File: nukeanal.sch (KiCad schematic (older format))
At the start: 84 parts, among them K1 CONN_3, P1 BNC, P4 CONN_2, Q1 VN3205N8-G, Q2 MMBT5089, Q3 LP0701, Q4 MMBT5089, Q5 BSS83, Q6 BSS83, SW1 ONOFF, U1 OPA2365, U10 74HC14, U11 74HC74, U2 LE33CD, U3 MIC5219YM5TR, U4 REF5045, U5 MIC5209-2.5, U6 OPA2365, U7 74HC14, U8 LM311N, U9 AD7983

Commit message: jerry fixed regulator
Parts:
- removed U2: LE33CD, Power_Integrations:SO-8, symbol LE33-SO8
- added P?: CONN_1, symbol CONN_1
- added P?: CONN_6, symbol CONN_6
- added P?: DE-9F, symbol CONN_9
- added U2: MIC5209-3.3, 111kicad-jake:SOT-223-3, symbol 7805
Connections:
- net +5.15V is gone; now on net +5.25V: CU4.1, U4.2 (VIN)
- net +3.3V: now also U2.VO
- net BATT+: now also U2.VI; no longer U3.1 (VIN)
- net GND: now also P?.1, P?.1 (P1), P?.2, P?.2 (P2), P?.3 (P3), P?.4 (P4), P?.5 (P5), U2.GND
- net SCLK: now also P?.4, P?.7 (P7)
- net SDO: now also P?.3, P?.6 (P6)
- net TEST: now also P?.1
- net ~CE: now also P?.5, P?.8 (P8)
- net ~REQ: now also P?.6, P?.9 (P9)
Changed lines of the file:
@@
 TEMP
-$Comp
-L +5.15V #PWR11
-U 1 1 534107A8
-P 4100 1500
-F 0 "#PWR11" H 4100 1460 30  0001 C CNN
-F 1 "+5.15V" H 4100 1610 30  0000 C CNN
-F 2 "" H 4100 1500 60  0001 C CNN
-F 3 "" H 4100 1500 60  0000 C CNN
-	1    4100 1500
-	1    0    0    -1
-$EndComp
 $Comp
 L C C3
@@
 L GND #PWR8
 U 1 1 53410E43
-P 3500 5200
-F 0 "#PWR8" H 3500 5200 30  0001 C CNN
-F 1 "GND" H 3500 5130 30  0001 C CNN
-F 2 "" H 3500 5200 60  0001 C CNN
-F 3 "" H 3500 5200 60  0000 C CNN
-	1    3500 5200
+P 3200 5150
+F 0 "#PWR8" H 3200 5150 30  0001 C CNN
+F 1 "GND" H 3200 5080 30  0001 C CNN
+F 2 "" H 3200 5150 60  0001 C CNN
+F 3 "" H 3200 5150 60  0000 C CNN
+	1    3200 5150
 	1    0    0    -1
 $EndComp
@@
 Text Notes 13750 4650 0    60   ~ 0
 Spare
-$Comp
-L LE33-SO8 U2
-U 1 1 534125E6
-P 3200 4950
-F 0 "U2" H 3200 4650 60  0000 C CNN
-F 1 "LE33CD" H 3200 5150 60  0000 C CNN
-F 2 "Power_Integrations:SO-8" H 3200 4950 60  0001 C CNN
-F 3 "" H 3200 4950 60  0000 C CNN
-	1    3200 4950
-	1    0    0    -1
-$EndComp
-$Comp
-L GND #PWR5
-U 1 1 53412625
-P 2750 5050
-F 0 "#PWR5" H 2750 5050 30  0001 C CNN
-F 1 "GND" H 2750 4980 30  0001 C CNN
-F 2 "" H 2750 5050 60  0001 C CNN
-F 3 "" H 2750 5050 60  0000 C CNN
-	1    2750 5050
-	1    0    0    -1
-$EndComp
 Text Notes 3850 5600 0    60   ~ 0
 change to 5.25v Vdd and -0.25v Vee
@@
 	7350 3750 8300 3750
 Wire Wire Line
-	7350 3350 7100 3350
+	7100 3350 7350 3350
 Wire Wire Line
 	8150 2750 8150 3550
@@
 Wire Wire Line
 	3650 1500 4350 1500
-Connection ~ 2900 5050
-Connection ~ 3500 5050
-Connection ~ 3500 5150
-Wire Wire Line
-	3500 4950 3500 5200
 Wire Wire Line
 	6200 2800 6200 3350
-Wire Wire Line
-	3500 4850 4100 4850
 Wire Wire Line
 	4000 4950 4100 4950
@@
 Wire Wire Line
 	5900 1650 5900 1400
-Wire Wire Line
-	2900 4950 2900 5050
-Wire Wire Line
-	2900 5050 2750 5050
-Wire Wire Line
-	2800 4850 2900 4850
 Wire Wire Line
 	4100 5050 3850 5050
@@
 Wire Wire Line
 	850  3350 1500 3350
+$Comp
+L +5.25V #PWR?
+U 1 1 534622F8
+P 4100 1500
+F 0 "#PWR?" H 4100 1630 20  0001 C CNN
+F 1 "+5.25V" H 4100 1600 30  0000 C CNN
+F 2 "" H 4100 1500 60  0000 C CNN
+F 3 "" H 4100 1500 60  0000 C CNN
+	1    4100 1500
+	1    0    0    -1
+$EndComp
+$Comp
+L 7805 U2
+U 1 1 5346230A
+P 3200 4900
+F 0 "U2" H 3350 4704 60  0000 C CNN
+F 1 "MIC5209-3.3" H 3200 5100 60  0000 C CNN
+F 2 "111kicad-jake:SOT-223-3" H 3200 4550 60  0001 C CNN
+F 3 "" H 3200 4900 60  0000 C CNN
+	1    3200 4900
+	-1   0    0    -1
+$EndComp
+Wire Wire Line
+	3850 4850 3600 4850
+$Comp
+L CONN_1 P?
+U 1 1 53462529
+P 13600 2900
+F 0 "P?" H 13680 2900 40  0000 L CNN
+F 1 "CONN_1" H 13600 2955 30  0001 C CNN
+F 2 "" H 13600 2900 60  0000 C CNN
+F 3 "" H 13600 2900 60  0000 C CNN
+	1    13600 2900
+	0    1    1    0
+$EndComp
+$Comp
+L CONN_6 P?
+U 1 1 534625CF
+P 15700 4900
+F 0 "P?" V 15650 4900 60  0000 C CNN
+F 1 "CONN_6" V 15750 4900 60  0000 C CNN
+F 2 "" H 15700 4900 60  0000 C CNN
+F 3 "" H 15700 4900 60  0000 C CNN
+	1    15700 4900
+	1    0    0    -1
+$EndComp
+$Comp
+L CONN_9 P?
+U 1 1 53462603
+P 15750 3950
+F 0 "P?" V 15700 3950 60  0000 C CNN
+F 1 "DE-9F" V 15800 3950 60  0000 C CNN
+F 2 "" H 15750 3950 60  0000 C CNN
+F 3 "" H 15750 3950 60  0000 C CNN
+	1    15750 3950
+	1    0    0    -1
+$EndComp
+Text Label 14900 5050 2    60   ~ 0
+~CE
+Wire Wire Line
+	14900 5050 15350 5050
+Text Label 15200 4950 2    60   ~ 0
+SCLK
+Wire Wire Line
+	15350 4950 15200 4950
+Text Label 14750 4850 2    60   ~ 0
+SDO
+Wire Wire Line
+	14750 4850 15350 4850
+Text Label 15050 5200 2    60   ~ 0
+~REQ
+Wire Wire Line
+	15050 5200 15350 5200
+Wire Wire Line
+	15350 5200 15350 5150
+$Comp
+L GND #PWR?
+U 1 1 53462BE7
+P 15200 4650
+F 0 "#PWR?" H 15200 4650 30  0001 C CNN
+F 1 "GND" H 15200 4580 30  0001 C CNN
+F 2 "" H 15200 4650 60  0000 C CNN
+F 3 "" H 15200 4650 60  0000 C CNN
+	1    15200 4650
+	1    0    0    -1
+$EndComp
+Wire Wire Line
+	15200 4650 15350 4650
+Wire Wire Line
+	15350 4650 15350 4750
+Connection ~ 15350 4650
+Text Label 15150 4050 2    60   ~ 0
+SDO
+Wire Wire Line
+	15150 4050 15400 4050
+$Comp
+L GND #PWR?
+U 1 1 53462E3D
+P 15250 3600
+F 0 "#PWR?" H 15250 3600 30  0001 C CNN
+F 1 "GND" H 15250 3530 30  0001 C CNN
+F 2 "" H 15250 3600 60  0000 C CNN
+F 3 "" H 15250 3600 60  0000 C CNN
+	1    15250 3600
+	1    0    0    -1
+$EndComp
+Wire Wire Line
+	15250 3600 15400 3600
+Wire Wire Line
+	15400 3550 15400 3950
+Connection ~ 15400 3650
+Connection ~ 15400 3750
+Connection ~ 15400 3850
+Connection ~ 15400 3950
+Connection ~ 15400 3600
+Connection ~ 15400 3550
+Text Label 15100 4150 2    60   ~ 0
+SCLK
+Wire Wire Line
+	15100 4150 15400 4150
+Text Label 15100 4250 2    60   ~ 0
+~CE
+Wire Wire Line
+	15100 4250 15400 4250
+Text Label 15150 4400 2    60   ~ 0
+~REQ
+Wire Wire Line
+	15150 4400 15400 4400
+Wire Wire Line
+	15400 4400 15400 4350
 $EndSCHEMATC

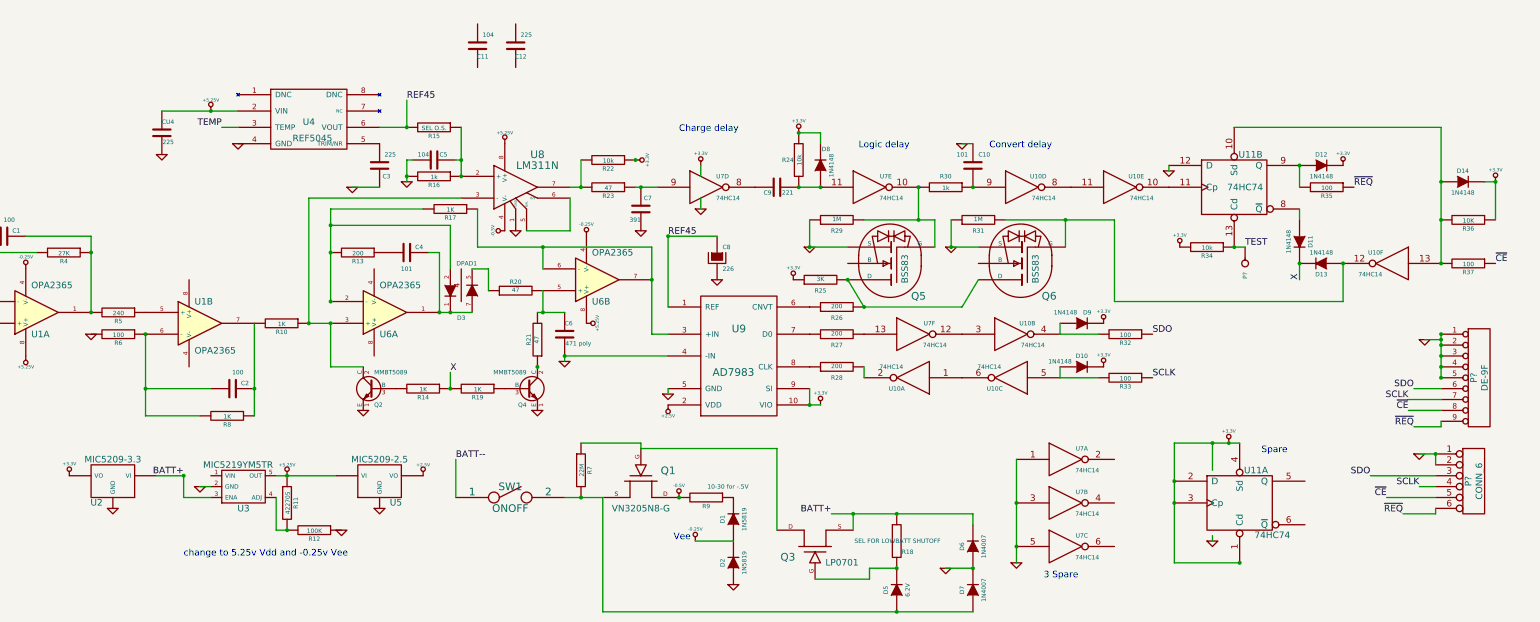
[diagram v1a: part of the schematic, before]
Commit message: leaving jerry to lay out the board, after autoplacing
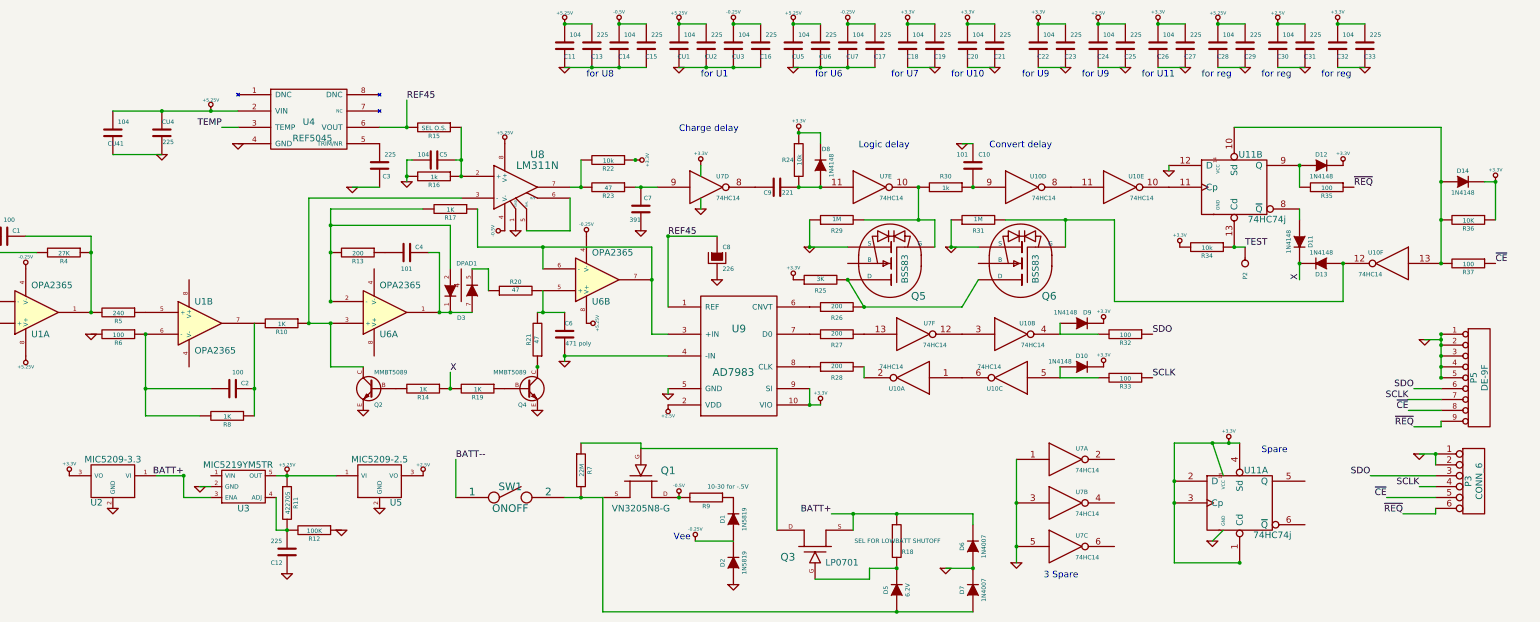
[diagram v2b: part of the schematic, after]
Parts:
- removed Q2, Q4: MMBT5089, Housings_SOT-23_SOT-143_TSOT-6:SOT23_Transistor_BC846_Handsoldering_RevB_14Mar2014, symbol 2SC1941
- removed U11: 74HC74, SMD_Packages:SO14N, symbol 74HC74
- removed U2: MIC5209-3.3, 111kicad-jake:SOT-223-3, symbol 7805
- removed U5: MIC5209-2.5, 111kicad-jake:SOT-223-3, symbol 7805
- added C13, C15, C16, C17, C19, C21, C23, C25, C27, C29, C31, C33, CU2, CU6: 225, SMD_Packages:SM0805, symbol C
- added C14, C18, C20, C22, C24, C26, C28, C30, C32, CU1, CU3, CU41, CU5, CU7: 104, SMD_Packages:SM0805, symbol C
- added Q2, Q4: MMBT5089, symbol MMBT5089
- added U11: 74HC74j, SMD_Packages:SO14N, symbol 74HC74j
- added U2: MIC5209-3.3, symbol MIC5209
- added U5: MIC5209-2.5, symbol MIC5209
- P2: renamed from P?; footprint (none) -> 111kicad-jerry:testpin037
- P3: renamed from P?; footprint (none) -> 111kicad-jerry:6x1pin037
- P5: renamed from P?; footprint (none) -> 111kicad-jerry:DB9FC
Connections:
- net +2.5V: now also C24.2, C25.2, C30.2, C31.2, U5.3 (VO)
- net +3.3V: now also C18.2, C19.2, C20.2, C21.2, C22.2, C23.2, C26.2, C27.2, C32.2, C33.2, U11.1 (Cd), U11.14 (VCC), U11.2 (D), U11.3 (Cp), U11.4 (Sd), U2.3 (VO)
- net +5.25V: now also C11.2, C13.2, C28.2, C29.2, CU1.2, CU2.2, CU41.2, CU5.2, CU6.2, U5.1 (VI)
- net -0.25V: now also C16.2, C17.2, CU3.2, CU7.2
- net -0.5V: now also C14.2, C15.2
- net BATT+: now also U2.1 (VI)
- net GND: now also C11.1, C12.1, C13.1, C14.1, C15.1, C16.1, C17.1, C18.1, C19.1, C20.1, C21.1, C22.1, C23.1, C24.1, C25.1, C26.1, C27.1, C28.1, C29.1, C30.1, C31.1, C32.1, C33.1, CU1.1, CU2.1, CU3.1, CU41.1, CU5.1, CU6.1, CU7.1, Q2.E, Q4.E, U11.12 (D), U11.7 (GND), U2.2 (GND), U5.2 (GND)
- net TEST: now also U11.13 (Cd)
- net at U10.10: now also U11.11 (Cp)
- net at D14.1 (A), R36.2, R37.2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: now also U11.10 (Sd)
- net at D11.1 (A): now also U11.8 (~Q)
- net at D12.1 (A), R35.2: now also U11.9 (Q)
- net at R10.1, U6.3 (+), U8.3 (-): now also Q2.C
- net at R21.1: now also Q4.C
- net at R19.1: now also Q4.B
- net at R14.2: now also Q2.B
- net at R11.2, R12.2, U3.4 (ADJ): now also C12.2
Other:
- note added: "for U1"
- note added: "for U10"
- note added: "for U11"
- note added: "for U6"
- note added: "for U7"
- note added: "for U8"
- note added: "for U9"
- note added: "for reg"
- note removed: "change to 5.25v Vdd and -0.25v Vee"
- moved on the sheet: C12
